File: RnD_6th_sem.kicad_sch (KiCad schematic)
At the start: 60 parts, among them IC1 2EDF7275KXUMA1, J1 HVDC1, J2 PWM, J3 HVDC2, J4 3.3V, J5 5V, J6 5V, J7 GND2, J8 GND1, Q1 IGLD60R190D1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

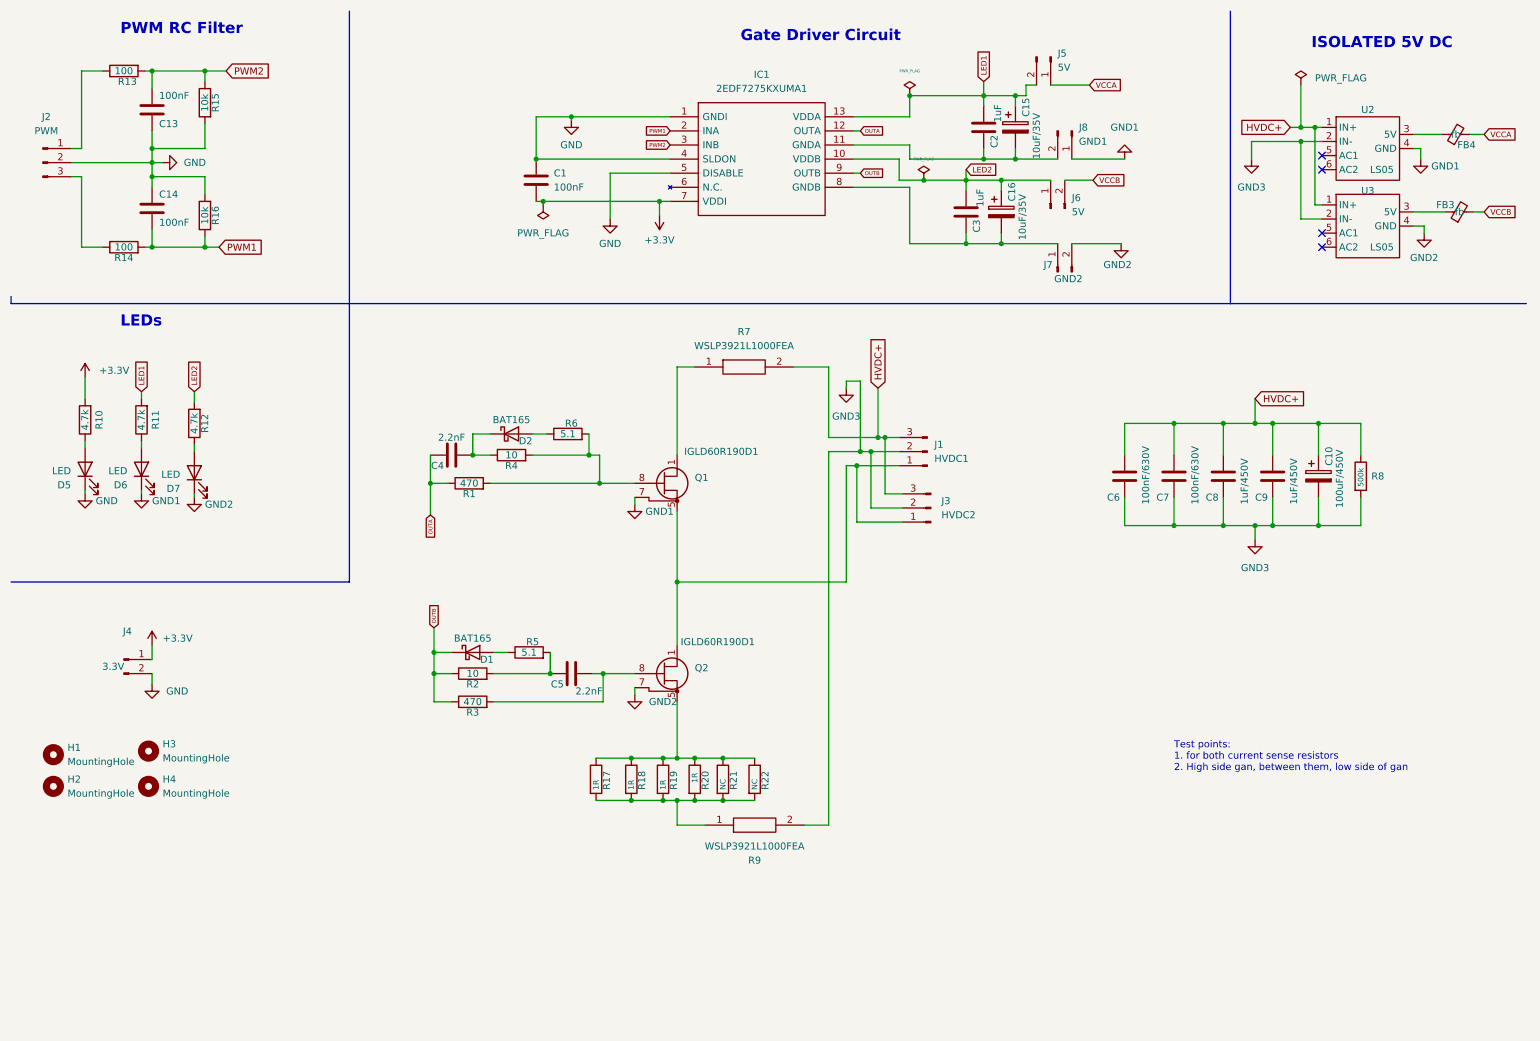
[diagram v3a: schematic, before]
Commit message: updated the schematic
removed the mmcx connector resistors
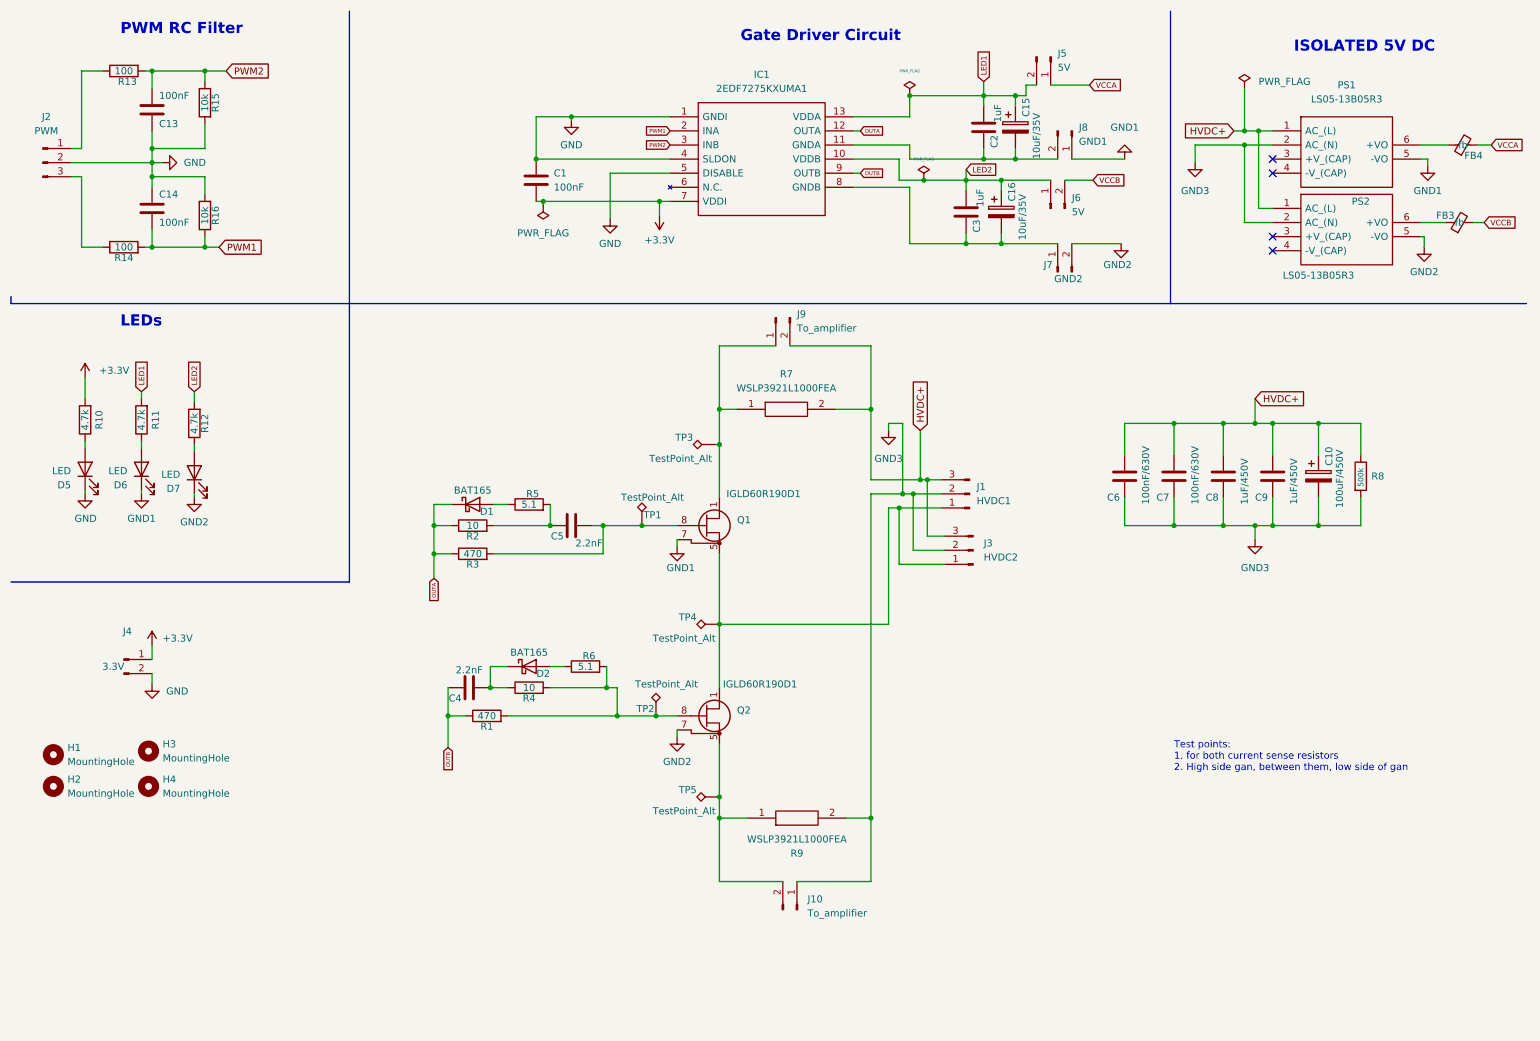
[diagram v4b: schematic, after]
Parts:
- removed R17, R18, R19, R20: 1R, Resistor_SMD:R_0805_2012Metric, symbol Device:R
- removed R21, R22: NC, Resistor_SMD:R_0805_2012Metric, symbol Device:R
- removed U2, U3: LS05, symbol DC-DC Powersupply:LS05
- added J10, J9: To_amplifier, Connector_Molex:Molex_KK-254_AE-6410-02A_1x02_P2.54mm_Vertical, symbol Connector:Conn_01x02_Male
- added PS1, PS2: LS05-13B05R3, footprint&lib:LS0513B05R3, symbol LS05-13B05R3:LS05-13B05R3
- added TP1, TP2, TP3, TP4, TP5: TestPoint_Alt, TestPoint:TestPoint_THTPad_1.5x1.5mm_Drill0.7mm, symbol Connector:TestPoint_Alt
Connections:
- net GND1: now also PS1.5 (-VO)
- net GND2: now also PS2.5 (-VO)
- net GND3: now also J10.1 (Pin_1), PS1.2 (AC_(N)), PS2.2 (AC_(N))
- net HVDC+: now also J9.2 (Pin_2), PS1.1 (AC_(L)), PS2.1 (AC_(L))
- net OUTA: now also D1.1 (K), R2.1, R3.1; no longer C4.1, R1.1
- net OUTB: now also C4.1, R1.1; no longer D1.1 (K), R2.1, R3.1
- net at J1.1 (Pin_1), J3.1 (Pin_1), Q1.5 (S)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: now also TP4.1
- net at FB4.1: now also PS1.6 (+VO)
- net at C5.2, R3.2: now also Q1.8 (G), TP1.1; no longer Q2.8 (G)
- net at Q2.5 (S), Q2.6 (S), Q2.9 (S): now also R9.1, J10.2 (Pin_2), TP5.1
- net at R1.2, R4.2, R6.2: now also Q2.8 (G), TP2.1; no longer Q1.8 (G)
- net at FB3.1: now also PS2.6 (+VO)
- net at Q1.1 (D), Q1.2 (D), Q1.3 (D)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: now also J9.1 (Pin_1), TP3.1
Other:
- moved on the sheet: C4, C5, D1, D2, FB3, FB4, J1, J3, Q1, Q2, R1, R2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
